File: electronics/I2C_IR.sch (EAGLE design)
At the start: 10 parts

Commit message: Revised board layout
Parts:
- renumbered U$1 to U1
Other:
- moved on the sheet: JP1, SJ1, SJ2
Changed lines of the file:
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@@
 <part name="C4" library="rcl" deviceset="C-US" device="C0603" value="10uF"/>
 <part name="P+4" library="supply1" deviceset="VCC" device="" value="5V"/>
-<part name="U$1" library="mes_adc" deviceset="ADC081C021" device=""/>
-<part name="P+1" library="supply1" deviceset="VCC" device="" value="5V"/>
+<part name="U1" library="mes_adc" deviceset="ADC081C021" device=""/>
 <part name="C1" library="rcl" deviceset="C-US" device="C0603" value="4.7uF"/>
 <part name="JP1" library="pinhead-2" deviceset="PINHD-1X04" device="_2.54-S" value="MCU"/>
@@
 <part name="SUPPLY3" library="supply2" deviceset="GND" device=""/>
 <part name="SUPPLY4" library="supply2" deviceset="GND" device=""/>
+<part name="P+1" library="supply1" deviceset="VCC" device="" value="5V"/>
 </parts>
 <sheets>
@@
 <instance part="C4" gate="G$1" x="154.94" y="88.9"/>
 <instance part="P+4" gate="VCC" x="154.94" y="116.84"/>
-<instance part="U$1" gate="G$1" x="91.44" y="91.44" rot="R180"/>
-<instance part="P+1" gate="VCC" x="60.96" y="119.38" rot="MR0"/>
+<instance part="U1" gate="G$1" x="91.44" y="91.44" rot="R180"/>
 <instance part="C1" gate="G$1" x="48.26" y="93.98" rot="MR0"/>
-<instance part="JP1" gate="A" x="177.8" y="66.04"/>
-<instance part="SUPPLY2" gate="GND" x="167.64" y="55.88" rot="MR0"/>
-<instance part="P+2" gate="VCC" x="167.64" y="78.74" rot="MR0"/>
-<instance part="SJ1" gate="G$1" x="88.9" y="129.54"/>
-<instance part="SJ2" gate="G$1" x="106.68" y="129.54" rot="MR0"/>
-<instance part="P+3" gate="VCC" x="88.9" y="142.24" rot="MR0"/>
-<instance part="P+5" gate="VCC" x="106.68" y="142.24"/>
-<instance part="SUPPLY3" gate="GND" x="88.9" y="116.84" rot="MR0"/>
-<instance part="SUPPLY4" gate="GND" x="106.68" y="116.84"/>
+<instance part="JP1" gate="A" x="96.52" y="139.7" rot="MR0"/>
+<instance part="SUPPLY2" gate="GND" x="106.68" y="124.46"/>
+<instance part="P+2" gate="VCC" x="106.68" y="157.48" rot="MR0"/>
+<instance part="SJ1" gate="G$1" x="96.52" y="45.72"/>
+<instance part="SJ2" gate="G$1" x="119.38" y="45.72" rot="MR0"/>
+<instance part="P+3" gate="VCC" x="96.52" y="58.42" rot="MR0"/>
+<instance part="P+5" gate="VCC" x="119.38" y="58.42"/>
+<instance part="SUPPLY3" gate="GND" x="96.52" y="33.02" rot="MR0"/>
+<instance part="SUPPLY4" gate="GND" x="119.38" y="33.02"/>
+<instance part="P+1" gate="VCC" x="60.96" y="119.38"/>
 </instances>
 <busses>
@@
 </segment>
 <segment>
-<pinref part="U$1" gate="G$1" pin="VA"/>
-<pinref part="P+1" gate="VCC" pin="VCC"/>
+<pinref part="JP1" gate="A" pin="1"/>
+<wire x1="99.06" y1="144.78" x2="106.68" y2="144.78" width="0.1524" layer="91"/>
+<wire x1="106.68" y1="144.78" x2="106.68" y2="154.94" width="0.1524" layer="91"/>
+<pinref part="P+2" gate="VCC" pin="VCC"/>
+</segment>
+<segment>
+<pinref part="SJ1" gate="G$1" pin="1"/>
+<pinref part="P+3" gate="VCC" pin="VCC"/>
+<wire x1="96.52" y1="55.88" x2="96.52" y2="50.8" width="0.1524" layer="91"/>
+</segment>
+<segment>
+<pinref part="SJ2" gate="G$1" pin="1"/>
+<pinref part="P+5" gate="VCC" pin="VCC"/>
+<wire x1="119.38" y1="55.88" x2="119.38" y2="50.8" width="0.1524" layer="91"/>
+</segment>
+<segment>
+<pinref part="U1" gate="G$1" pin="VA"/>
 <wire x1="76.2" y1="99.06" x2="60.96" y2="99.06" width="0.1524" layer="91"/>
 <wire x1="60.96" y1="99.06" x2="60.96" y2="116.84" width="0.1524" layer="91"/>
@@
 <wire x1="60.96" y1="99.06" x2="48.26" y2="99.06" width="0.1524" layer="91"/>
 <wire x1="48.26" y1="99.06" x2="48.26" y2="96.52" width="0.1524" layer="91"/>
-</segment>
-<segment>
-<pinref part="JP1" gate="A" pin="1"/>
-<wire x1="175.26" y1="71.12" x2="167.64" y2="71.12" width="0.1524" layer="91"/>
-<wire x1="167.64" y1="71.12" x2="167.64" y2="76.2" width="0.1524" layer="91"/>
-<pinref part="P+2" gate="VCC" pin="VCC"/>
-</segment>
-<segment>
-<pinref part="SJ1" gate="G$1" pin="1"/>
-<pinref part="P+3" gate="VCC" pin="VCC"/>
-<wire x1="88.9" y1="139.7" x2="88.9" y2="134.62" width="0.1524" layer="91"/>
-</segment>
-<segment>
-<pinref part="SJ2" gate="G$1" pin="1"/>
-<pinref part="P+5" gate="VCC" pin="VCC"/>
-<wire x1="106.68" y1="139.7" x2="106.68" y2="134.62" width="0.1524" layer="91"/>
+<pinref part="P+1" gate="VCC" pin="VCC"/>
 </segment>
 </net>
@@
 <pinref part="SUPPLY1" gate="GND" pin="GND"/>
 <pinref part="C2" gate="G$1" pin="2"/>
-<pinref part="U$1" gate="G$1" pin="GND"/>
+<pinref part="U1" gate="G$1" pin="GND"/>
 <wire x1="60.96" y1="76.2" x2="60.96" y2="68.58" width="0.1524" layer="91"/>
 <wire x1="76.2" y1="88.9" x2="60.96" y2="88.9" width="0.1524" layer="91"/>
@@
 <segment>
 <pinref part="JP1" gate="A" pin="4"/>
-<wire x1="175.26" y1="63.5" x2="167.64" y2="63.5" width="0.1524" layer="91"/>
-<wire x1="167.64" y1="63.5" x2="167.64" y2="58.42" width="0.1524" layer="91"/>
+<wire x1="99.06" y1="137.16" x2="106.68" y2="137.16" width="0.1524" layer="91"/>
+<wire x1="106.68" y1="137.16" x2="106.68" y2="127" width="0.1524" layer="91"/>
 <pinref part="SUPPLY2" gate="GND" pin="GND"/>
 </segment>
@@
 <pinref part="SJ1" gate="G$1" pin="3"/>
 <pinref part="SUPPLY3" gate="GND" pin="GND"/>
-<wire x1="88.9" y1="119.38" x2="88.9" y2="124.46" width="0.1524" layer="91"/>
+<wire x1="96.52" y1="35.56" x2="96.52" y2="40.64" width="0.1524" layer="91"/>
 </segment>
 <segment>
 <pinref part="SJ2" gate="G$1" pin="3"/>
 <pinref part="SUPPLY4" gate="GND" pin="GND"/>
-<wire x1="106.68" y1="119.38" x2="106.68" y2="124.46" width="0.1524" layer="91"/>
+<wire x1="119.38" y1="35.56" x2="119.38" y2="40.64" width="0.1524" layer="91"/>
 </segment>
 </net>
@@
 <net name="SDA" class="0">
 <segment>
-<pinref part="U$1" gate="G$1" pin="SDA"/>
+<pinref part="U1" gate="G$1" pin="SDA"/>
 <wire x1="76.2" y1="83.82" x2="66.04" y2="83.82" width="0.1524" layer="91"/>
 <label x="66.04" y="83.82" size="1.778" layer="95"/>
@@
 <segment>
 <pinref part="JP1" gate="A" pin="3"/>
-<wire x1="175.26" y1="66.04" x2="160.02" y2="66.04" width="0.1524" layer="91"/>
-<label x="160.02" y="66.04" size="1.778" layer="95"/>
+<wire x1="99.06" y1="139.7" x2="114.3" y2="139.7" width="0.1524" layer="91"/>
+<label x="114.3" y="139.7" size="1.778" layer="95" rot="MR0"/>
 </segment>
 </net>
@@
 <pinref part="C3" gate="G$1" pin="1"/>
 <junction x="124.46" y="99.06"/>
-<pinref part="U$1" gate="G$1" pin="VIN"/>
+<pinref part="U1" gate="G$1" pin="VIN"/>
 <wire x1="106.68" y1="99.06" x2="124.46" y2="99.06" width="0.1524" layer="91"/>
 </segment>
@@
 <net name="SCL" class="0">
 <segment>
-<pinref part="U$1" gate="G$1" pin="SCL"/>
+<pinref part="U1" gate="G$1" pin="SCL"/>
 <wire x1="106.68" y1="83.82" x2="116.84" y2="83.82" width="0.1524" layer="91"/>
 <label x="116.84" y="83.82" size="1.778" layer="95" rot="MR0"/>
@@
 <segment>
 <pinref part="JP1" gate="A" pin="2"/>
-<wire x1="175.26" y1="68.58" x2="160.02" y2="68.58" width="0.1524" layer="91"/>
-<label x="160.02" y="68.58" size="1.778" layer="95"/>
+<wire x1="99.06" y1="142.24" x2="114.3" y2="142.24" width="0.1524" layer="91"/>
+<label x="114.3" y="142.24" size="1.778" layer="95" rot="MR0"/>
 </segment>
 </net>
 <net name="ADR1" class="0">
 <segment>
-<pinref part="U$1" gate="G$1" pin="ADR1"/>
+<pinref part="U1" gate="G$1" pin="ADR1"/>
 <wire x1="76.2" y1="93.98" x2="66.04" y2="93.98" width="0.1524" layer="91"/>
 <label x="66.04" y="93.98" size="1.778" layer="95"/>
@@
 <segment>
 <pinref part="SJ2" gate="G$1" pin="2"/>
-<wire x1="111.76" y1="129.54" x2="119.38" y2="129.54" width="0.1524" layer="91"/>
-<label x="119.38" y="129.54" size="1.778" layer="95" rot="MR0"/>
+<wire x1="124.46" y1="45.72" x2="132.08" y2="45.72" width="0.1524" layer="91"/>
+<label x="132.08" y="45.72" size="1.778" layer="95" rot="MR0"/>
 </segment>
 </net>
 <net name="ADR0" class="0">
 <segment>
-<pinref part="U$1" gate="G$1" pin="ADR0"/>
+<pinref part="U1" gate="G$1" pin="ADR0"/>
 <wire x1="106.68" y1="93.98" x2="116.84" y2="93.98" width="0.1524" layer="91"/>
 <label x="116.84" y="93.98" size="1.778" layer="95" rot="MR0"/>
@@
 <segment>
 <pinref part="SJ1" gate="G$1" pin="2"/>
-<wire x1="83.82" y1="129.54" x2="76.2" y2="129.54" width="0.1524" layer="91"/>
-<label x="76.2" y="129.54" size="1.778" layer="95"/>
+<wire x1="91.44" y1="45.72" x2="83.82" y2="45.72" width="0.1524" layer="91"/>
+<label x="83.82" y="45.72" size="1.778" layer="95"/>
 </segment>
 </net>
 <net name="ALERT" class="0">
 <segment>
-<pinref part="U$1" gate="G$1" pin="ALERT"/>
+<pinref part="U1" gate="G$1" pin="ALERT"/>
 <wire x1="106.68" y1="88.9" x2="116.84" y2="88.9" width="0.1524" layer="91"/>
 <label x="116.84" y="88.9" size="1.778" layer="95" rot="MR0"/>

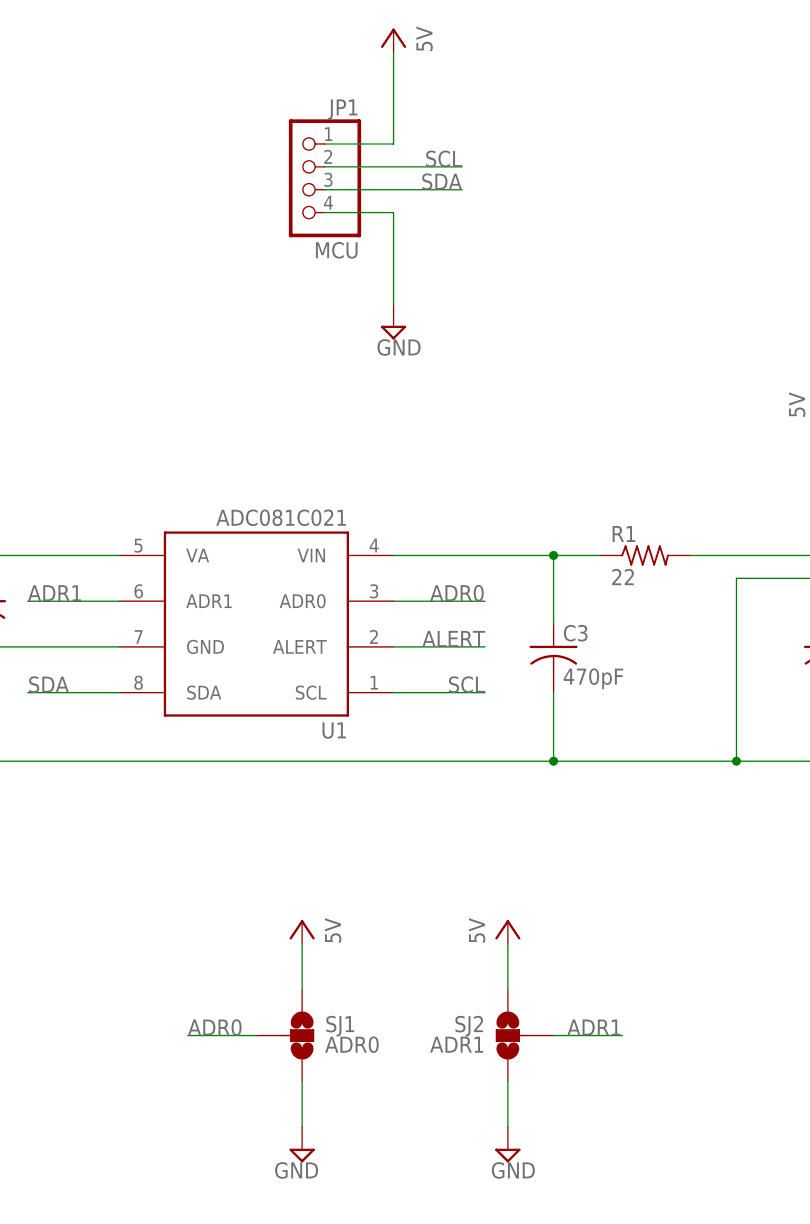
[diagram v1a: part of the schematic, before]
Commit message: Revised board layout per datasheet, single ground plane with join at chip ground location, no bottom traces, use tantalum bypass caps, etc.
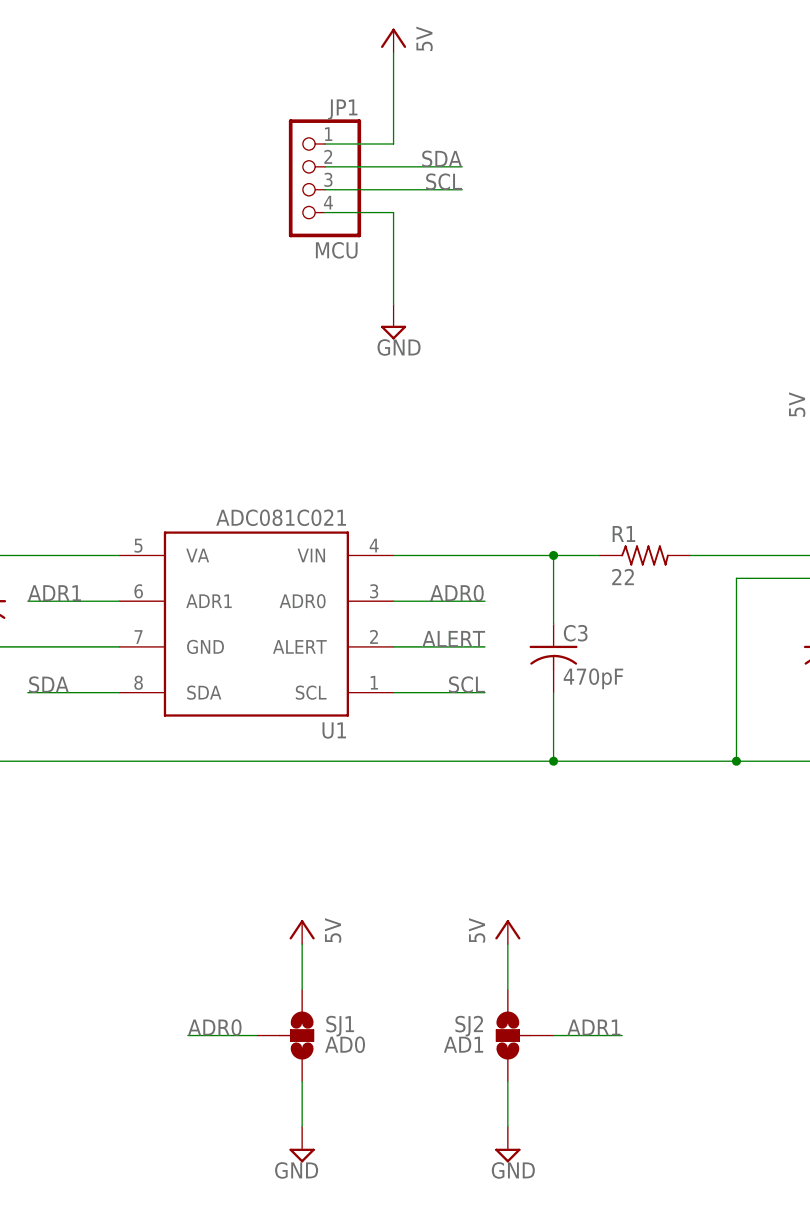
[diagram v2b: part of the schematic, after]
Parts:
- C1: device rcl:C-USC0603 -> rcl:C-USC0805K; PARTNO (none) -> T491A475K010AT
- C4: device rcl:C-USC0603 -> rcl:C-USC0805K
- SJ1: value ADR0 -> AD0
- SJ2: value ADR1 -> AD1
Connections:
- net SCL: now also JP1.3; no longer JP1.2
- net SDA: now also JP1.2; no longer JP1.3
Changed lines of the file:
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@@
 <grid distance="0.1" unitdist="inch" unit="inch" style="lines" multiple="1" display="no" altdistance="0.01" altunitdist="inch" altunit="inch"/>
 <layers>
-<layer number="1" name="Top" color="4" fill="1" visible="no" active="no"/>
-<layer number="16" name="Bottom" color="1" fill="1" visible="no" active="no"/>
-<layer number="17" name="Pads" color="2" fill="1" visible="no" active="no"/>
-<layer number="18" name="Vias" color="2" fill="1" visible="no" active="no"/>
-<layer number="19" name="Unrouted" color="6" fill="1" visible="no" active="no"/>
-<layer number="20" name="Dimension" color="15" fill="1" visible="no" active="no"/>
-<layer number="21" name="tPlace" color="7" fill="1" visible="no" active="no"/>
-<layer number="22" name="bPlace" color="7" fill="1" visible="no" active="no"/>
-<layer number="23" name="tOrigins" color="15" fill="1" visible="no" active="no"/>
-<layer number="24" name="bOrigins" color="15" fill="1" visible="no" active="no"/>
-<layer number="25" name="tNames" color="7" fill="1" visible="no" active="no"/>
-<layer number="26" name="bNames" color="7" fill="1" visible="no" active="no"/>
-<layer number="27" name="tValues" color="7" fill="1" visible="no" active="no"/>
-<layer number="28" name="bValues" color="7" fill="1" visible="no" active="no"/>
+<layer number="1" name="Top" color="4" fill="1" visible="yes" active="no"/>
+<layer number="16" name="Bottom" color="1" fill="1" visible="yes" active="no"/>
+<layer number="17" name="Pads" color="2" fill="1" visible="yes" active="no"/>
+<layer number="18" name="Vias" color="2" fill="1" visible="yes" active="no"/>
+<layer number="19" name="Unrouted" color="6" fill="1" visible="yes" active="no"/>
+<layer number="20" name="Dimension" color="15" fill="1" visible="yes" active="no"/>
+<layer number="21" name="tPlace" color="7" fill="1" visible="yes" active="no"/>
+<layer number="22" name="bPlace" color="7" fill="1" visible="yes" active="no"/>
+<layer number="23" name="tOrigins" color="15" fill="1" visible="yes" active="no"/>
+<layer number="24" name="bOrigins" color="15" fill="1" visible="yes" active="no"/>
+<layer number="25" name="tNames" color="7" fill="1" visible="yes" active="no"/>
+<layer number="26" name="bNames" color="7" fill="1" visible="yes" active="no"/>
+<layer number="27" name="tValues" color="7" fill="1" visible="yes" active="no"/>
+<layer number="28" name="bValues" color="7" fill="1" visible="yes" active="no"/>
 <layer number="29" name="tStop" color="7" fill="3" visible="no" active="no"/>
 <layer number="30" name="bStop" color="7" fill="6" visible="no" active="no"/>
@@
 <layer number="35" name="tGlue" color="7" fill="4" visible="no" active="no"/>
 <layer number="36" name="bGlue" color="7" fill="5" visible="no" active="no"/>
-<layer number="37" name="tTest" color="7" fill="1" visible="no" active="no"/>
-<layer number="38" name="bTest" color="7" fill="1" visible="no" active="no"/>
+<layer number="37" name="tTest" color="7" fill="1" visible="yes" active="no"/>
+<layer number="38" name="bTest" color="7" fill="1" visible="yes" active="no"/>
 <layer number="39" name="tKeepout" color="4" fill="11" visible="no" active="no"/>
 <layer number="40" name="bKeepout" color="1" fill="11" visible="no" active="no"/>
@@
 <layer number="44" name="Drills" color="7" fill="1" visible="no" active="no"/>
 <layer number="45" name="Holes" color="7" fill="1" visible="no" active="no"/>
-<layer number="46" name="Milling" color="3" fill="1" visible="no" active="no"/>
-<layer number="47" name="Measures" color="7" fill="1" visible="no" active="no"/>
-<layer number="48" name="Document" color="7" fill="1" visible="no" active="no"/>
-<layer number="49" name="Reference" color="7" fill="1" visible="no" active="no"/>
-<layer number="50" name="dxf" color="7" fill="1" visible="no" active="no"/>
-<layer number="51" name="tDocu" color="7" fill="1" visible="no" active="no"/>
-<layer number="52" name="bDocu" color="7" fill="1" visible="no" active="no"/>
-<layer number="53" name="tPadExt" color="7" fill="1" visible="no" active="no"/>
-<layer number="54" name="bPadExt" color="1" fill="1" visible="no" active="no"/>
-<layer number="56" name="wert" color="7" fill="1" visible="no" active="no"/>
+<layer number="46" name="Milling" color="3" fill="1" visible="yes" active="no"/>
+<layer number="47" name="Measures" color="7" fill="1" visible="yes" active="no"/>
+<layer number="48" name="Document" color="7" fill="1" visible="yes" active="no"/>
+<layer number="49" name="Reference" color="7" fill="1" visible="yes" active="no"/>
+<layer number="50" name="dxf" color="7" fill="1" visible="yes" active="no"/>
+<layer number="51" name="tDocu" color="7" fill="1" visible="yes" active="no"/>
+<layer number="52" name="bDocu" color="7" fill="1" visible="yes" active="no"/>
+<layer number="53" name="tPadExt" color="7" fill="1" visible="yes" active="no"/>
+<layer number="54" name="bPadExt" color="1" fill="1" visible="yes" active="no"/>
+<layer number="56" name="wert" color="7" fill="1" visible="yes" active="no"/>
 <layer number="91" name="Nets" color="2" fill="1" visible="yes" active="yes"/>
 <layer number="92" name="Busses" color="1" fill="1" visible="yes" active="yes"/>
@@
 <part name="FRAME1" library="mes" deviceset="LETTER_L" device=""/>
 <part name="JP3" library="pinhead-2" deviceset="PINHD-1X03" device="_2.00" value="Sharp Module"/>
-<part name="C4" library="rcl" deviceset="C-US" device="C0603" value="10uF"/>
+<part name="C4" library="rcl" deviceset="C-US" device="C0805K" value="10uF"/>
 <part name="P+4" library="supply1" deviceset="VCC" device="" value="5V"/>
 <part name="U1" library="mes_adc" deviceset="ADC081C021" device=""/>
-<part name="C1" library="rcl" deviceset="C-US" device="C0603" value="4.7uF"/>
+<part name="C1" library="rcl" deviceset="C-US" device="C0805K" value="4.7uF">
+<attribute name="PARTNO" value="T491A475K010AT"/>
+</part>
 <part name="JP1" library="pinhead-2" deviceset="PINHD-1X04" device="_2.54-S" value="MCU"/>
 <part name="SUPPLY2" library="supply2" deviceset="GND" device=""/>
 <part name="P+2" library="supply1" deviceset="VCC" device="" value="5V"/>
-<part name="SJ1" library="SparkFun" deviceset="SOLDERJUMPER_2WAY" device="S" value="ADR0"/>
-<part name="SJ2" library="SparkFun" deviceset="SOLDERJUMPER_2WAY" device="S" value="ADR1"/>
+<part name="SJ1" library="SparkFun" deviceset="SOLDERJUMPER_2WAY" device="S" value="AD0"/>
+<part name="SJ2" library="SparkFun" deviceset="SOLDERJUMPER_2WAY" device="S" value="AD1"/>
 <part name="P+3" library="supply1" deviceset="VCC" device="" value="5V"/>
 <part name="P+5" library="supply1" deviceset="VCC" device="" value="5V"/>
@@
 <instance part="P+4" gate="VCC" x="154.94" y="116.84"/>
 <instance part="U1" gate="G$1" x="91.44" y="91.44" rot="R180"/>
-<instance part="C1" gate="G$1" x="48.26" y="93.98" rot="MR0"/>
+<instance part="C1" gate="G$1" x="48.26" y="93.98" rot="MR0">
+<attribute name="PARTNO" x="48.26" y="93.98" size="1.778" layer="96" display="off"/>
+</instance>
 <instance part="JP1" gate="A" x="96.52" y="139.7" rot="MR0"/>
 <instance part="SUPPLY2" gate="GND" x="106.68" y="124.46"/>
@@
 </segment>
 <segment>
-<pinref part="JP1" gate="A" pin="3"/>
-<wire x1="99.06" y1="139.7" x2="114.3" y2="139.7" width="0.1524" layer="91"/>
-<label x="114.3" y="139.7" size="1.778" layer="95" rot="MR0"/>
+<pinref part="JP1" gate="A" pin="2"/>
+<wire x1="99.06" y1="142.24" x2="114.3" y2="142.24" width="0.1524" layer="91"/>
+<label x="114.3" y="142.24" size="1.778" layer="95" rot="MR0"/>
 </segment>
 </net>
@@
 </segment>
 <segment>
-<pinref part="JP1" gate="A" pin="2"/>
-<wire x1="99.06" y1="142.24" x2="114.3" y2="142.24" width="0.1524" layer="91"/>
-<label x="114.3" y="142.24" size="1.778" layer="95" rot="MR0"/>
-</segment>
-</net>
+<pinref part="JP1" gate="A" pin="3"/>
+<wire x1="99.06" y1="139.7" x2="114.3" y2="139.7" width="0.1524" layer="91"/>
+<label x="114.3" y="139.7" size="1.778" layer="95" rot="MR0"/>
+</segment>
+</net>
